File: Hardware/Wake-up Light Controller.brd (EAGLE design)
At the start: 85.7 x 54 mm, 47 parts, among them IC1 ST1S10, IC2 HT7333, IC3 DS3231/SO, IC4 ATMEGA328P_TQFP, J1 AVR-ISP, J2 Debug, Q1 BSS138, Q2 BSS138, Q3 FDN306P, Q4 IRLZ44N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

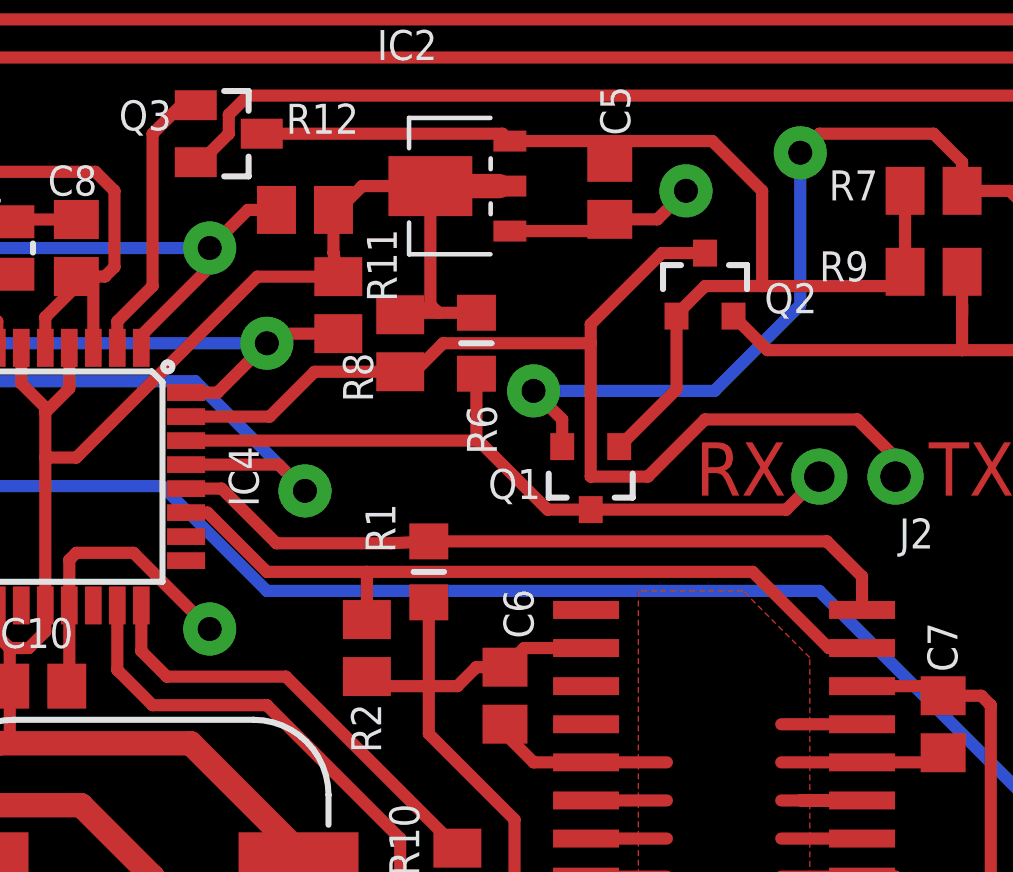
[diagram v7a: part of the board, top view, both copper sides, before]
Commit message: Changed resistor pad spacing
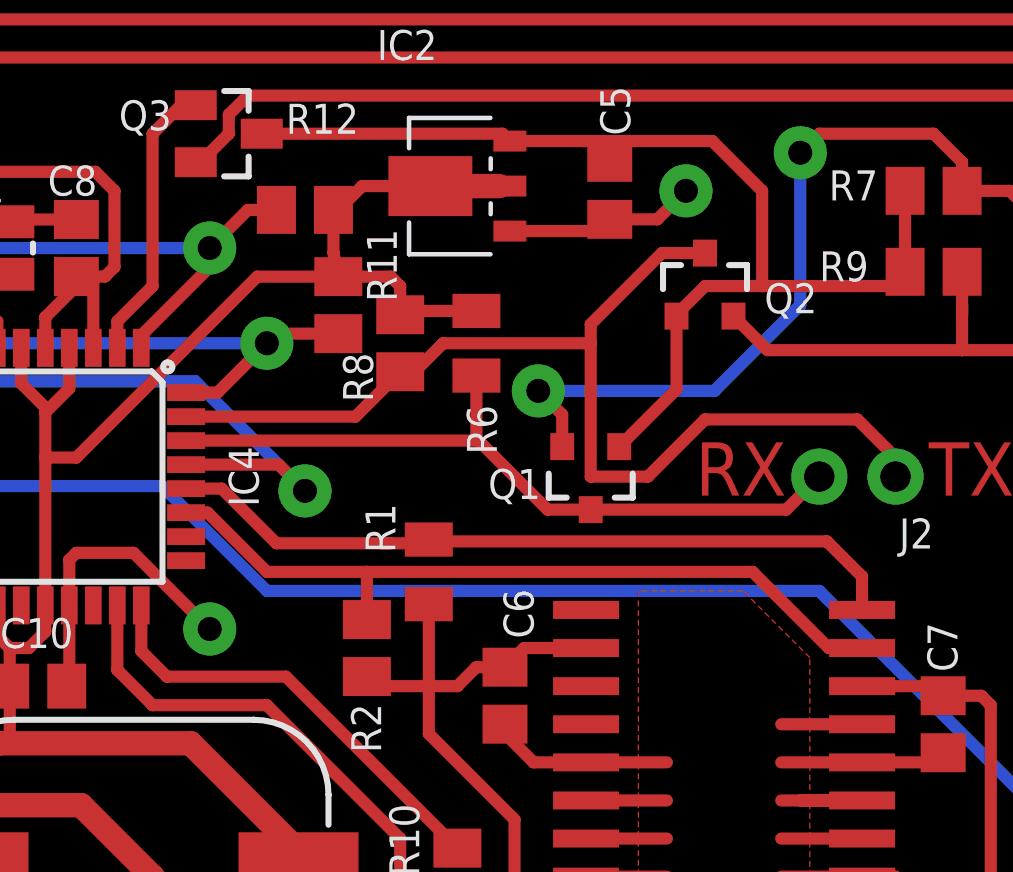
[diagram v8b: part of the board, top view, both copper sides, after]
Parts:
- R1, R6: device rc-master-smd:R0805MP -> heol:M0805
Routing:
- net +5V: track 158.2 -> 157.0 mm
- net SCL: track 24.9 -> 25.4 mm
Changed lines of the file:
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@@
 <attribute name="VALUE" x="5.3975" y="13.335" size="1" layer="27" rot="R90"/>
 </element>
-<element name="R1" library="rc-master-smd" package="R0805MP" value="4.7k" x="34.6075" y="33.02" smashed="yes" rot="R90">
+<element name="R1" library="heol" package="M0805" value="4.7k" x="34.6075" y="33.02" smashed="yes" rot="R90">
 <attribute name="NAME" x="33.49625" y="33.655" size="1" layer="25" rot="R90"/>
 <attribute name="VALUE" x="36.5125" y="32.7025" size="1" layer="27" rot="R90"/>
@@
 <attribute name="VALUE" x="40.005" y="35.179" size="1" layer="27" font="vector" ratio="11" align="top-center"/>
 </element>
-<element name="R6" library="rc-master-smd" package="R0805MP" value="10k" x="36.195" y="40.64" smashed="yes" rot="R270">
+<element name="R6" library="heol" package="M0805" value="10k" x="36.195" y="40.64" smashed="yes" rot="R270">
 <attribute name="NAME" x="35.8775" y="38.57625" size="1" layer="25" rot="R270"/>
 <attribute name="VALUE" x="36.83" y="42.38625" size="1" layer="27" rot="R270"/>
@@
 <wire x1="26.5176" y1="35.795" x2="27.705" y2="35.795" width="0.4064" layer="1"/>
 <wire x1="27.705" y1="35.795" x2="29.5275" y2="33.9725" width="0.4064" layer="1"/>
-<wire x1="29.5275" y1="33.9725" x2="33.335" y2="33.9725" width="0.4064" layer="1"/>
-<wire x1="33.335" y1="33.9725" x2="34.6075" y2="34.036" width="0.4064" layer="1"/>
+<wire x1="29.5275" y1="33.9725" x2="33.02" y2="33.9725" width="0.4064" layer="1"/>
+<wire x1="33.02" y1="33.9725" x2="33.335" y2="33.9725" width="0.4064" layer="1"/>
 <wire x1="49.05" y1="31.75" x2="49.05" y2="32.865" width="0.4064" layer="1"/>
 <wire x1="49.05" y1="32.865" x2="47.879" y2="34.036" width="0.4064" layer="1"/>
-<wire x1="47.879" y1="34.036" x2="34.6075" y2="34.036" width="0.4064" layer="1"/>
+<wire x1="34.483" y1="33.9725" x2="33.02" y2="33.9725" width="0.4064" layer="1"/>
+<wire x1="34.483" y1="33.9725" x2="34.6075" y2="34.097" width="0.4064" layer="1"/>
+<wire x1="47.879" y1="34.036" x2="34.5465" y2="34.036" width="0.4064" layer="1"/>
+<wire x1="34.5465" y1="34.036" x2="34.483" y2="33.9725" width="0.4064" layer="1"/>
 </signal>
 <signal name="SDA">
@@
 <contactref element="U1" pad="1"/>
 <contactref element="R7" pad="2"/>
-<wire x1="39.055" y1="37.195" x2="39.055" y2="38.1025" width="0.4064" layer="1"/>
-<wire x1="39.055" y1="38.1025" x2="38.1" y2="39.0525" width="0.4064" layer="1"/>
-<via x="38.1" y="39.0525" extent="1-16" drill="0.8" diameter="1.778"/>
+<wire x1="39.055" y1="37.195" x2="39.055" y2="38.26125" width="0.4064" layer="1"/>
+<wire x1="39.055" y1="38.26125" x2="38.25875" y2="39.0525" width="0.4064" layer="1"/>
+<via x="38.25875" y="39.0525" extent="1-16" drill="0.8" diameter="1.778"/>
 <via x="46.99" y="46.99" extent="1-16" drill="0.8" diameter="1.778"/>
 <wire x1="51.435" y1="47.625" x2="47.625" y2="47.625" width="0.4064" layer="1"/>
@@
 <wire x1="52.385" y1="46.675" x2="52.385" y2="45.72" width="0.4064" layer="1"/>
 <wire x1="52.385" y1="46.675" x2="51.435" y2="47.625" width="0.4064" layer="1"/>
-<wire x1="38.1" y1="39.0525" x2="44.1325" y2="39.0525" width="0.4064" layer="16"/>
+<wire x1="38.25875" y1="39.0525" x2="44.1325" y2="39.0525" width="0.4064" layer="16"/>
 <wire x1="44.1325" y1="39.0525" x2="46.99" y2="41.91" width="0.4064" layer="16"/>
 <wire x1="46.99" y1="41.91" x2="46.99" y2="46.99" width="0.4064" layer="16"/>
@@
 <contactref element="Q2" pad="3"/>
 <contactref element="R8" pad="2"/>
-<wire x1="29.305" y1="38.195" x2="26.5176" y2="38.195" width="0.4064" layer="1"/>
-<wire x1="30.8" y1="39.69" x2="33.655" y2="39.69" width="0.4064" layer="1"/>
-<wire x1="30.8" y1="39.69" x2="29.305" y2="38.195" width="0.4064" layer="1"/>
-<wire x1="33.655" y1="39.69" x2="33.975" y2="39.69" width="0.4064" layer="1"/>
-<wire x1="33.655" y1="39.69" x2="34.13375" y2="39.69" width="0.4064" layer="1"/>
+<wire x1="32.1625" y1="38.195" x2="26.5176" y2="38.195" width="0.4064" layer="1"/>
+<wire x1="33.6575" y1="39.69" x2="32.1625" y2="38.195" width="0.4064" layer="1"/>
+<wire x1="33.6575" y1="39.69" x2="34.13375" y2="39.69" width="0.4064" layer="1"/>
+<wire x1="33.655" y1="39.69" x2="33.6575" y2="39.69" width="0.4064" layer="1"/>
 <wire x1="34.13375" y1="39.69" x2="35.08375" y2="40.64" width="0.4064" layer="1"/>
 <wire x1="40.005" y1="40.64" x2="40.005" y2="41.275" width="0.4064" layer="1"/>
@@
 <wire x1="33.655" y1="41.59" x2="33.39" y2="41.855" width="0.4064" layer="1"/>
 <wire x1="35.56" y1="29.21" x2="34.6075" y2="29.21" width="0.4064" layer="1"/>
-<wire x1="34.6075" y1="32.004" x2="34.6075" y2="29.21" width="0.4064" layer="1"/>
+<wire x1="34.6075" y1="31.943" x2="34.6075" y2="29.21" width="0.4064" layer="1"/>
 <wire x1="21.825" y1="31.9024" x2="21.825" y2="36.83" width="0.4064" layer="1"/>
 <wire x1="21.825" y1="36.83" x2="21.825" y2="38.335" width="0.4064" layer="1"/>
-<wire x1="34.925" y1="41.656" x2="36.195" y2="41.656" width="0.4064" layer="1"/>
-<wire x1="34.925" y1="41.656" x2="33.721" y2="41.656" width="0.4064" layer="1"/>
-<wire x1="33.721" y1="41.656" x2="33.655" y2="41.59" width="0.4064" layer="1"/>
 <wire x1="30.265" y1="21.59" x2="30.265" y2="23.71" width="0.8128" layer="1"/>
 <wire x1="30.265" y1="23.71" x2="26.67" y2="27.305" width="0.8128" layer="1"/>
@@
 <contactref element="R11" pad="1"/>
 <contactref element="R12" pad="1"/>
-<wire x1="34.66" y1="45.87875" x2="34.66" y2="41.921" width="0.4064" layer="1"/>
-<wire x1="34.66" y1="41.921" x2="34.925" y2="41.656" width="0.4064" layer="1"/>
 <wire x1="31.59125" y1="45.085" x2="31.43" y2="45.085" width="0.4064" layer="1"/>
 <wire x1="31.59125" y1="45.085" x2="32.385" y2="45.87875" width="0.4064" layer="1"/>
-<wire x1="31.59125" y1="42.86" x2="28.89" y2="42.86" width="0.4064" layer="1"/>
+<wire x1="28.89" y1="42.86" x2="31.59125" y2="42.86" width="0.4064" layer="1"/>
 <wire x1="28.89" y1="42.86" x2="22.86" y2="36.83" width="0.4064" layer="1"/>
 <wire x1="31.43" y1="45.085" x2="31.43" y2="43.65625" width="0.4064" layer="1"/>
@@
 <wire x1="30.265" y1="14.605" x2="30.265" y2="13.12" width="0.4064" layer="1"/>
 <wire x1="34.29" y1="14.605" x2="30.265" y2="14.605" width="0.4064" layer="1"/>
+<wire x1="36.195" y1="41.717" x2="33.782" y2="41.717" width="0.4064" layer="1"/>
+<wire x1="33.782" y1="41.717" x2="33.655" y2="41.59" width="0.4064" layer="1"/>
+<wire x1="31.59125" y1="42.86" x2="33.34" y2="42.86" width="0.4064" layer="1"/>
+<wire x1="33.34" y1="42.86" x2="33.655" y2="42.545" width="0.4064" layer="1"/>
+<wire x1="33.655" y1="42.545" x2="33.655" y2="41.59" width="0.4064" layer="1"/>
 </signal>
 <signal name="N$7">
@@
 <contactref element="Q1" pad="3"/>
 <contactref element="R6" pad="2"/>
-<wire x1="36.195" y1="37.465" x2="36.195" y2="39.624" width="0.4064" layer="1"/>
+<wire x1="36.195" y1="37.465" x2="36.195" y2="39.563" width="0.4064" layer="1"/>
 <wire x1="36.265" y1="37.395" x2="36.195" y2="37.465" width="0.4064" layer="1"/>
 <wire x1="26.5176" y1="37.395" x2="36.265" y2="37.395" width="0.4064" layer="1"/>
